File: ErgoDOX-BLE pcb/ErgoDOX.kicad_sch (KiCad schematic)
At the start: 97 parts, among them J1 Conn_01x04, J2 Conn_01x02_Female, J3 Conn_01x02_Female, J4 Conn_01x02, J5 Conn_01x02, P1 USB_C_Plug_USB2.0, SW0:10 SW0:3, SW0:11 SW0:2, SW0:12 SW0:1, SW0:7 SW0:6, SW0:8 SW0:5, SW0:9 SW0:4, SW1:10 SW1:3, SW1:11 SW1:2, SW1:12 SW1:1, SW1:13 SW1:0, SW1:9 SW1:4, SW2:10 SW2:3, SW2:11 SW2:2, SW2:12 SW2:1, SW2:13 SW2:0, SW2:7 SW2:6, SW2:8 SW2:5, SW2:9 SW2:4, SW3:10 SW3:3, SW3:11 SW3:2, SW3:12 SW3:1, SW3:13 SW3:0, SW3:8 SW3:5, SW3:9 SW3:4, SW4:10 SW4:3, SW4:11 SW4:2, SW4:12 SW4:1, SW4:13 SW4:0, SW4:7 SW4:6, SW4:8 SW4:5, SW4:9 SW4:4, SW5:10 SW5:3, SW5:11 SW5:2, SW5:12 SW5:1, SW5:13 SW5:0, SW5:7 SW5:6, SW5:8 SW5:5, SW5:9 SW5:4, U1 MCP23018

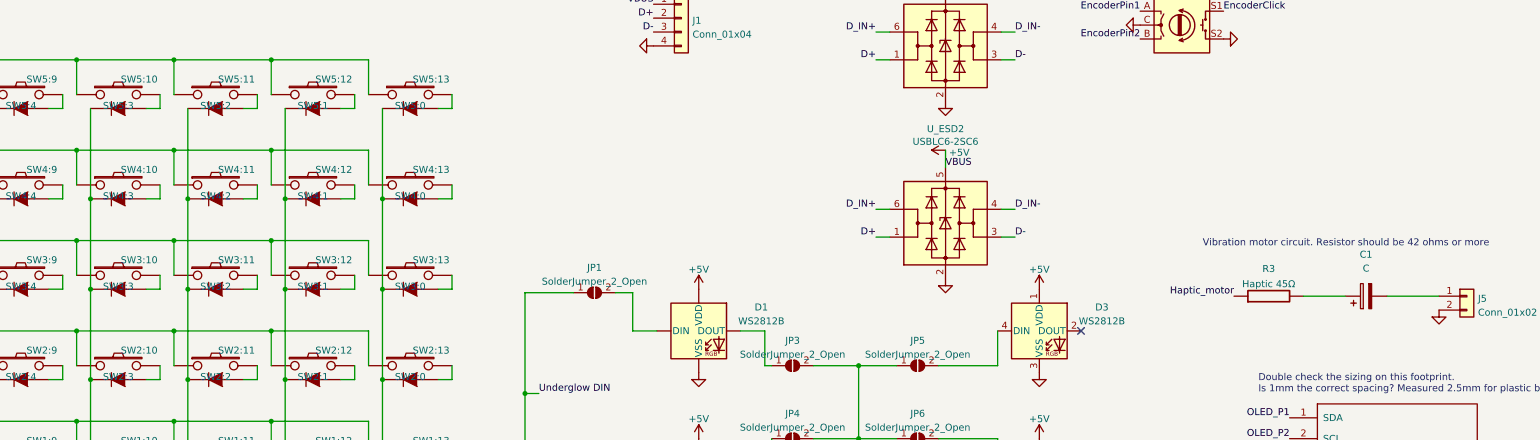
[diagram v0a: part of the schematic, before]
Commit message: Add transistor to haptic feedback curcuit
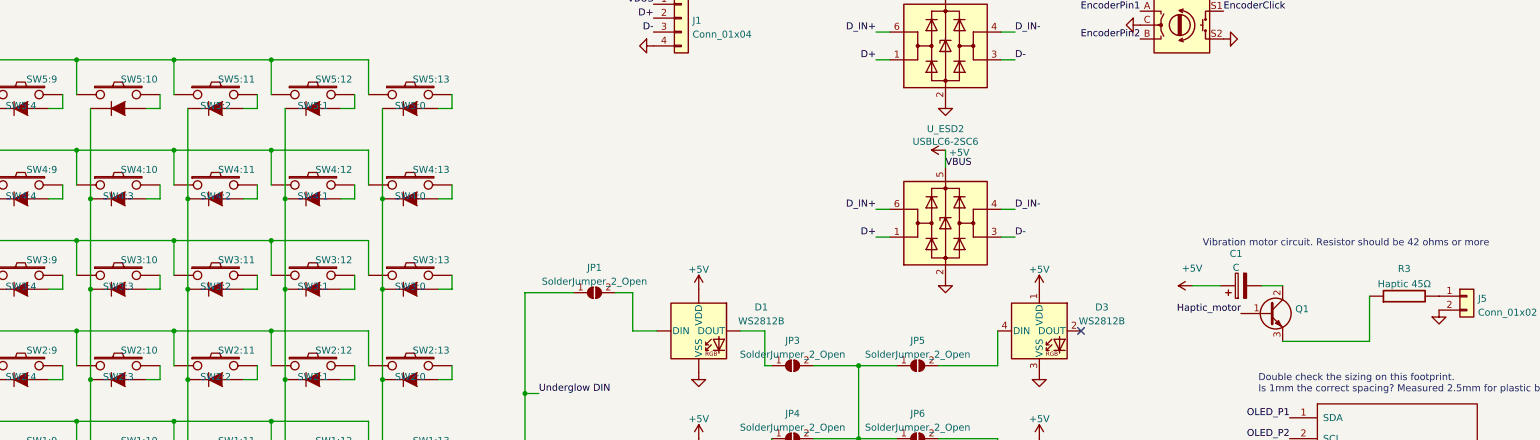
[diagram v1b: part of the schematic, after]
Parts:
- added Q1: (no value), symbol Device:Q_NPN_BCE
- SW5:10: value SW5:3 -> (none); footprint ErgoDOX pcb:MX_FLIP_DIODE_HOTSWAP -> (none)
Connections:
- net +5V: now also C1.1
- net Haptic_motor: now also Q1.1 (B); no longer R3.1
- net at R3.2: now also J5.1 (Pin_1); no longer C1.1
- net at C1.2: now also Q1.2 (C); no longer J5.1 (Pin_1)
- new net: Q1.3 (E), R3.1
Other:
- moved on the sheet: C1, R3
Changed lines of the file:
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@@
     (stroke (width 0) (type default) (color 0 0 0 0))
   )
+  (wire (pts (xy 314.325 198.755) (xy 330.2 198.755))
+    (stroke (width 0) (type default) (color 0 0 0 0))
+  )
   (wire (pts (xy 142.24 222.25) (xy 144.78 222.25))
     (stroke (width 0) (type default) (color 0 0 0 0))
@@
     (stroke (width 0) (type default) (color 0 0 0 0))
   )
+  (wire (pts (xy 330.2 198.755) (xy 330.2 190.5))
+    (stroke (width 0) (type default) (color 0 0 0 0))
+  )
   (wire (pts (xy 93.98 147.32) (xy 111.76 147.32))
     (stroke (width 0) (type default) (color 0 0 0 0))
@@
     (stroke (width 0) (type default) (color 0 0 0 0))
   )
-  (wire (pts (xy 333.375 190.5) (xy 342.9 190.5))
-    (stroke (width 0) (type default) (color 0 0 0 0))
-  )
   (wire (pts (xy 55.88 238.76) (xy 55.88 236.22))
     (stroke (width 0) (type default) (color 0 0 0 0))
@@
     (stroke (width 0) (type default) (color 0 0 0 0))
   )
-  (wire (pts (xy 318.135 190.5) (xy 325.755 190.5))
-    (stroke (width 0) (type default) (color 0 0 0 0))
-  )
   (wire (pts (xy 73.66 238.76) (xy 73.66 236.22))
     (stroke (width 0) (type default) (color 0 0 0 0))
@@
     (stroke (width 0) (type default) (color 0 0 0 0))
   )
+  (wire (pts (xy 297.815 188.595) (xy 302.895 188.595))
+    (stroke (width 0) (type default) (color 0 0 0 0))
+  )
   (wire (pts (xy 236.855 203.2) (xy 243.84 203.2))
     (stroke (width 0) (type default) (color 0 0 0 0))
@@
     (stroke (width 0) (type default) (color 0 0 0 0))
   )
+  (wire (pts (xy 310.515 188.595) (xy 314.325 188.595))
+    (stroke (width 0) (type default) (color 0 0 0 0))
+  )
   (wire (pts (xy 111.76 163.83) (xy 111.76 170.18))
     (stroke (width 0) (type default) (color 0 0 0 0))
@@
     (effects (font (size 1.27 1.27)) (justify left bottom))
   )
-  (label "Haptic_motor" (at 305.435 190.5 180)
+  (label "Haptic_motor" (at 306.705 193.675 180)
     (effects (font (size 1.27 1.27)) (justify right bottom))
   )
@@
     (pin "4")
   )
-  (symbol (lib_id "component:SWITCH_DIODE") (at 101.6 153.67 0) (unit 1)
+  (symbol (lib_name "SWITCH_DIODE_1") (lib_id "component:SWITCH_DIODE") (at 101.6 153.67 0) (unit 1)
     (in_bom yes) (on_board yes)
     (property "Reference" "SW5:10" (id 0) (at 105.41 150.876 0))
-    (property "Value" "SW5:3" (id 1) (at 101.6 155.702 0))
-    (property "Footprint" "ErgoDOX pcb:MX_FLIP_DIODE_HOTSWAP" (id 2) (at 101.6 153.67 0)
+    (property "Value" "" (id 1) (at 101.6 155.702 0))
+    (property "Footprint" "" (id 2) (at 101.6 153.67 0)
       (effects (font (size 1.524 1.524)) hide)
     )
@@
     (pin "1")
   )
-  (symbol (lib_id "Device:C_Polarized") (at 329.565 190.5 90) (unit 1)
+  (symbol (lib_id "Device:C_Polarized") (at 306.705 188.595 90) (unit 1)
     (in_bom yes) (on_board yes) (fields_autoplaced)
-    (property "Reference" "C1" (id 0) (at 329.565 182.88 90))
-    (property "Value" "C" (id 1) (at 329.565 185.42 90))
-    (property "Footprint" "Capacitor_THT:C_Axial_L5.1mm_D3.1mm_P7.50mm_Horizontal" (id 2) (at 333.375 189.5348 0)
+    (property "Reference" "C1" (id 0) (at 305.816 182.7362 90))
+    (property "Value" "C" (id 1) (at 305.816 185.2731 90))
+    (property "Footprint" "Capacitor_THT:C_Axial_L5.1mm_D3.1mm_P7.50mm_Horizontal" (id 2) (at 310.515 187.6298 0)
       (effects (font (size 1.27 1.27)) hide)
     )
-    (property "Datasheet" "~" (id 3) (at 329.565 190.5 0)
+    (property "Datasheet" "~" (id 3) (at 306.705 188.595 0)
       (effects (font (size 1.27 1.27)) hide)
     )
@@
     (pin "4")
   )
+  (symbol (lib_id "Device:Q_NPN_BCE") (at 311.785 193.675 0) (unit 1)
+    (in_bom yes) (on_board yes) (fields_autoplaced)
+    (property "Reference" "Q1" (id 0) (at 316.6364 192.8403 0)
+      (effects (font (size 1.27 1.27)) (justify left))
+    )
+    (property "Value" "" (id 1) (at 316.6364 195.3772 0)
+      (effects (font (size 1.27 1.27)) (justify left))
+    )
+    (property "Footprint" "" (id 2) (at 316.865 191.135 0)
+      (effects (font (size 1.27 1.27)) hide)
+    )
+    (property "Datasheet" "~" (id 3) (at 311.785 193.675 0)
+      (effects (font (size 1.27 1.27)) hide)
+    )
+    (pin "1")
+    (pin "2")
+    (pin "3")
+  )
   (symbol (lib_id "Jumper:SolderJumper_2_Open") (at 358.14 238.125 0) (unit 1)
     (in_bom yes) (on_board yes)
@@
     (pin "1")
   )
+  (symbol (lib_id "power:+5V") (at 297.815 188.595 90) (unit 1)
+    (in_bom yes) (on_board yes)
+    (property "Reference" "#PWR017" (id 0) (at 301.625 188.595 0)
+      (effects (font (size 1.27 1.27)) hide)
+    )
+    (property "Value" "+5V" (id 1) (at 295.91 185.42 90)
+      (effects (font (size 1.27 1.27)) (justify right))
+    )
+    (property "Footprint" "" (id 2) (at 297.815 188.595 0)
+      (effects (font (size 1.27 1.27)) hide)
+    )
+    (property "Datasheet" "" (id 3) (at 297.815 188.595 0)
+      (effects (font (size 1.27 1.27)) hide)
+    )
+    (pin "1")
+  )
   (symbol (lib_id "power:+3V3") (at 106.68 44.45 0) (unit 1)
     (in_bom yes) (on_board yes) (fields_autoplaced)
@@
     (pin "9")
   )
-  (symbol (lib_id "component:RESISTOR") (at 311.785 190.5 90) (unit 1)
+  (symbol (lib_id "component:RESISTOR") (at 336.55 190.5 90) (unit 1)
     (in_bom yes) (on_board yes) (fields_autoplaced)
-    (property "Reference" "R3" (id 0) (at 311.785 185.4921 90))
-    (property "Value" "Haptic 45Ω" (id 1) (at 311.785 188.2672 90))
-    (property "Footprint" "ErgoDOX pcb:RESISTOR" (id 2) (at 311.785 190.5 0)
+    (property "Reference" "R3" (id 0) (at 336.55 185.4921 90))
+    (property "Value" "Haptic 45Ω" (id 1) (at 336.55 188.2672 90))
+    (property "Footprint" "ErgoDOX pcb:RESISTOR" (id 2) (at 336.55 190.5 0)
       (effects (font (size 1.27 1.27)) hide)
     )
-    (property "Datasheet" "" (id 3) (at 311.785 190.5 0)
+    (property "Datasheet" "" (id 3) (at 336.55 190.5 0)
       (effects (font (size 1.27 1.27)) hide)
     )
@@
       (reference "#PWR016") (unit 1) (value "+5V") (footprint "")
     )
+    (path "/74961e07-8ddd-425b-ae9d-7618b5d07f8c"
+      (reference "#PWR017") (unit 1) (value "+5V") (footprint "")
+    )
     (path "/b2ff08d7-b8f1-4672-b1f1-bb796fc3abc5"
       (reference "#PWR018") (unit 1) (value "GND") (footprint "")
@@
       (reference "P1") (unit 1) (value "USB_C_Plug_USB2.0") (footprint "Connector_USB:USB_C_Receptacle_GCT_USB4085")
     )
+    (path "/42f91f74-e2a0-4b26-ae70-d83777eb405b"
+      (reference "Q1") (unit 1) (value "Q_NPN_BCE") (footprint "Package_TO_SOT_SMD:SOT-23")
+    )
     (path "/00000000-0000-0000-0000-00004fd9dd65"

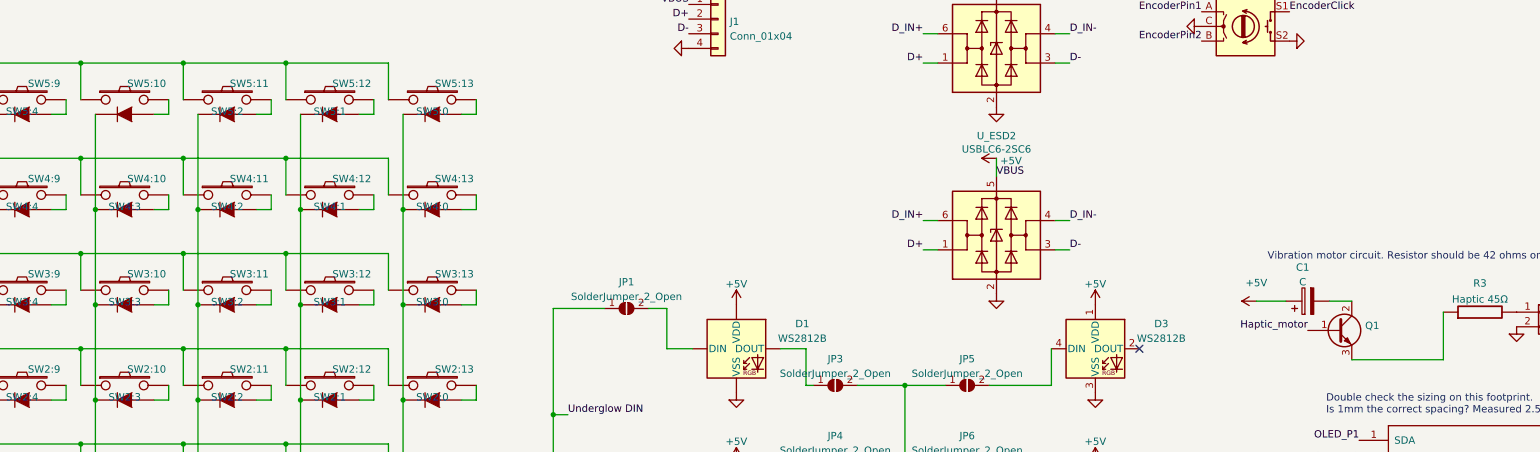
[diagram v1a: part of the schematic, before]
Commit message: Make the pads for kailh hot swaps the correct side
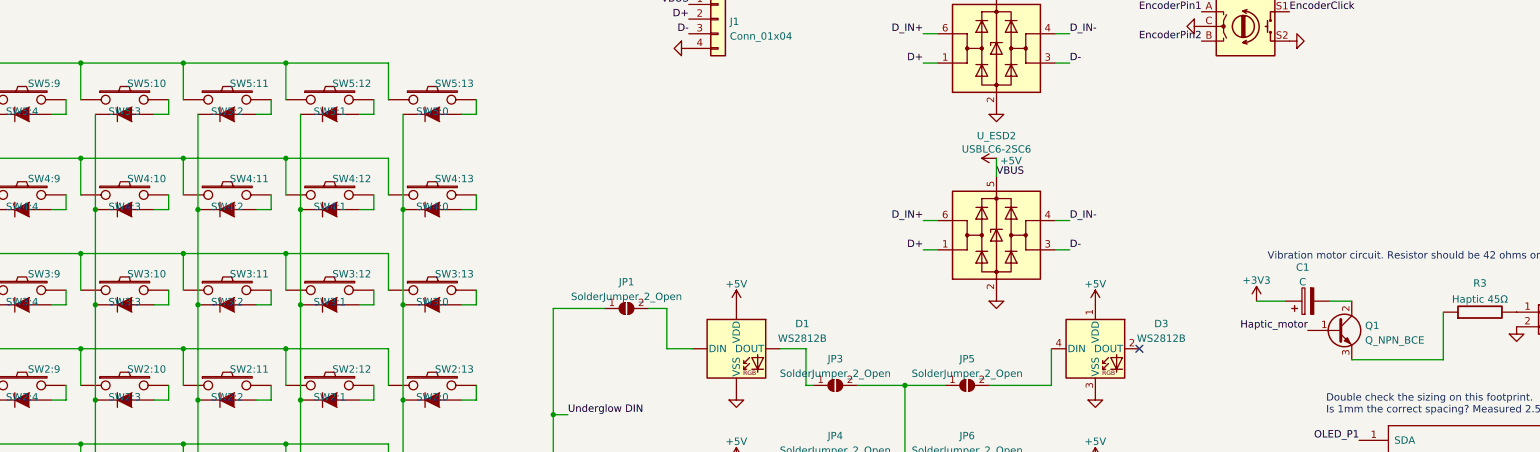
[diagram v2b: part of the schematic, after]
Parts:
- Q1: value (none) -> Q_NPN_BCE; footprint (none) -> Package_TO_SOT_SMD:SOT-23
- SW5:10: value (none) -> SW5:3; footprint (none) -> ErgoDOX pcb:MX_FLIP_DIODE_HOTSWAP
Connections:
- net +3V3: now also C1.1
- net +5V: no longer C1.1
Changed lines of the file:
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@@
     (in_bom yes) (on_board yes)
     (property "Reference" "SW5:10" (id 0) (at 105.41 150.876 0))
-    (property "Value" "" (id 1) (at 101.6 155.702 0))
-    (property "Footprint" "" (id 2) (at 101.6 153.67 0)
+    (property "Value" "SW5:3" (id 1) (at 101.6 155.702 0))
+    (property "Footprint" "ErgoDOX pcb:MX_FLIP_DIODE_HOTSWAP" (id 2) (at 101.6 153.67 0)
       (effects (font (size 1.524 1.524)) hide)
     )
@@
       (effects (font (size 1.27 1.27)) (justify left))
     )
-    (property "Value" "" (id 1) (at 316.6364 195.3772 0)
-      (effects (font (size 1.27 1.27)) (justify left))
-    )
-    (property "Footprint" "" (id 2) (at 316.865 191.135 0)
+    (property "Value" "Q_NPN_BCE" (id 1) (at 316.6364 195.3772 0)
+      (effects (font (size 1.27 1.27)) (justify left))
+    )
+    (property "Footprint" "Package_TO_SOT_SMD:SOT-23" (id 2) (at 316.865 191.135 0)
       (effects (font (size 1.27 1.27)) hide)
     )
@@
     )
     (property "Datasheet" "" (id 3) (at 361.95 238.125 0)
-      (effects (font (size 1.27 1.27)) hide)
-    )
-    (pin "1")
-  )
-  (symbol (lib_id "power:+5V") (at 297.815 188.595 90) (unit 1)
-    (in_bom yes) (on_board yes)
-    (property "Reference" "#PWR017" (id 0) (at 301.625 188.595 0)
-      (effects (font (size 1.27 1.27)) hide)
-    )
-    (property "Value" "+5V" (id 1) (at 295.91 185.42 90)
-      (effects (font (size 1.27 1.27)) (justify right))
-    )
-    (property "Footprint" "" (id 2) (at 297.815 188.595 0)
-      (effects (font (size 1.27 1.27)) hide)
-    )
-    (property "Datasheet" "" (id 3) (at 297.815 188.595 0)
       (effects (font (size 1.27 1.27)) hide)
     )
@@
     (pin "3")
     (pin "4")
+  )
+  (symbol (lib_id "power:+3V3") (at 297.815 188.595 0) (unit 1)
+    (in_bom yes) (on_board yes) (fields_autoplaced)
+    (property "Reference" "#PWR?" (id 0) (at 297.815 192.405 0)
+      (effects (font (size 1.27 1.27)) hide)
+    )
+    (property "Value" "+3V3" (id 1) (at 297.815 184.9905 0))
+    (property "Footprint" "" (id 2) (at 297.815 188.595 0)
+      (effects (font (size 1.27 1.27)) hide)
+    )
+    (property "Datasheet" "" (id 3) (at 297.815 188.595 0)
+      (effects (font (size 1.27 1.27)) hide)
+    )
+    (pin "1")
   )
   (symbol (lib_id "component:GND") (at 144.78 101.6 270) (unit 1)
@@
       (reference "#PWR016") (unit 1) (value "+5V") (footprint "")
     )
-    (path "/74961e07-8ddd-425b-ae9d-7618b5d07f8c"
-      (reference "#PWR017") (unit 1) (value "+5V") (footprint "")
-    )
     (path "/b2ff08d7-b8f1-4672-b1f1-bb796fc3abc5"
       (reference "#PWR018") (unit 1) (value "GND") (footprint "")
@@
       (reference "#PWR0107") (unit 1) (value "+5V") (footprint "")
     )
+    (path "/9262c7d3-8469-461f-b560-6292a46b6254"
+      (reference "#PWR?") (unit 1) (value "+3V3") (footprint "")
+    )
     (path "/dc3e5149-0691-4e48-82aa-18a33c58d220"

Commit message: Change edge switches to use the same footprint as the main ones and redo routes
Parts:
- SW2:13, SW3:13, SW4:13, SW5:13: footprint ErgoDOX pcb:MX_FLIP_XX -> ErgoDOX pcb:MX_FLIP_DIODE_HOTSWAP
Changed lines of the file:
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@@
     (property "Reference" "SW4:13" (id 0) (at 158.75 167.386 0))
     (property "Value" "SW4:0" (id 1) (at 154.94 172.212 0))
-    (property "Footprint" "ErgoDOX pcb:MX_FLIP_XX" (id 2) (at 154.94 170.18 0)
+    (property "Footprint" "ErgoDOX pcb:MX_FLIP_DIODE_HOTSWAP" (id 2) (at 154.94 170.18 0)
       (effects (font (size 1.524 1.524)) hide)
     )
@@
     (property "Reference" "SW3:13" (id 0) (at 158.75 183.896 0))
     (property "Value" "SW3:0" (id 1) (at 154.94 188.722 0))
-    (property "Footprint" "ErgoDOX pcb:MX_FLIP_XX" (id 2) (at 154.94 186.69 0)
+    (property "Footprint" "ErgoDOX pcb:MX_FLIP_DIODE_HOTSWAP" (id 2) (at 154.94 186.69 0)
       (effects (font (size 1.524 1.524)) hide)
     )
@@
     (property "Reference" "SW2:13" (id 0) (at 158.75 200.406 0))
     (property "Value" "SW2:0" (id 1) (at 154.94 205.232 0))
-    (property "Footprint" "ErgoDOX pcb:MX_FLIP_XX" (id 2) (at 154.94 203.2 0)
+    (property "Footprint" "ErgoDOX pcb:MX_FLIP_DIODE_HOTSWAP" (id 2) (at 154.94 203.2 0)
       (effects (font (size 1.524 1.524)) hide)
     )
@@
     (property "Reference" "SW5:13" (id 0) (at 158.75 150.876 0))
     (property "Value" "SW5:0" (id 1) (at 154.94 155.702 0))
-    (property "Footprint" "ErgoDOX pcb:MX_FLIP_XX" (id 2) (at 154.94 153.67 0)
+    (property "Footprint" "ErgoDOX pcb:MX_FLIP_DIODE_HOTSWAP" (id 2) (at 154.94 153.67 0)
       (effects (font (size 1.524 1.524)) hide)
     )
@@
     )
     (path "/00000000-0000-0000-0000-00004d92dfbb"
-      (reference "SW2:13") (unit 1) (value "SW2:0") (footprint "ErgoDOX pcb:MX_FLIP_XX")
+      (reference "SW2:13") (unit 1) (value "SW2:0") (footprint "ErgoDOX pcb:MX_FLIP_DIODE_HOTSWAP")
     )
     (path "/00000000-0000-0000-0000-00004d92df92"
@@
     )
     (path "/00000000-0000-0000-0000-00004d92dfad"
-      (reference "SW3:13") (unit 1) (value "SW3:0") (footprint "ErgoDOX pcb:MX_FLIP_XX")
+      (reference "SW3:13") (unit 1) (value "SW3:0") (footprint "ErgoDOX pcb:MX_FLIP_DIODE_HOTSWAP")
     )
     (path "/00000000-0000-0000-0000-00004d92df15"
@@
     )
     (path "/00000000-0000-0000-0000-00004d92df34"
-      (reference "SW4:13") (unit 1) (value "SW4:0") (footprint "ErgoDOX pcb:MX_FLIP_XX")
+      (reference "SW4:13") (unit 1) (value "SW4:0") (footprint "ErgoDOX pcb:MX_FLIP_DIODE_HOTSWAP")
     )
     (path "/00000000-0000-0000-0000-00004ffd34f8"
@@
     )
     (path "/00000000-0000-0000-0000-00004ffd34d4"
-      (reference "SW5:13") (unit 1) (value "SW5:0") (footprint "ErgoDOX pcb:MX_FLIP_XX")
+      (reference "SW5:13") (unit 1) (value "SW5:0") (footprint "ErgoDOX pcb:MX_FLIP_DIODE_HOTSWAP")
     )
     (path "/ad35f6b8-a74b-4a5d-8f87-06ce33e25a8f"
